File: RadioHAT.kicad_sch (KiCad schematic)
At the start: 37 parts, among them J1 RPi_GPIO, J3 Conn_02x06_Odd_Even, J4 Conn_02x07_Odd_Even, U1 INA219AxD, U2 LP3855-ADJ

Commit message: Rename footprint to match filter
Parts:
- R20: footprint RadioHAT:3362P1200LF -> RadioHAT:Potentiometer_Bourns_3362P1200LF
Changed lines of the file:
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@@
 			)
 		)
-		(property "Footprint" "RadioHAT:3362P1200LF"
+		(property "Footprint" "RadioHAT:Potentiometer_Bourns_3362P1200LF"
 			(at 91.44 151.13 0)
 			(effects

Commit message: Implemented @RemyChatel recommendations
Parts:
- removed C4, C5: 10u, Capacitor_Tantalum_SMD:CP_EIA-3216-18_Kemet-A, symbol Device:C_Polarized
- removed J3: Conn_02x06_Odd_Even, Connector_PinHeader_2.54mm:PinHeader_2x06_P2.54mm_Vertical, symbol Connector_Generic:Conn_02x06_Odd_Even
- removed JP4: SolderJumper_2_Open, Jumper:SolderJumper-2_P1.3mm_Open_Pad1.0x1.5mm, symbol Jumper:SolderJumper_2_Open
- added C4, C5: 100n, Capacitor_SMD:C_0805_2012Metric_Pad1.18x1.45mm_HandSolder, symbol Device:C
- added J3: Conn_02x07_Odd_Even, Connector_PinHeader_2.54mm:PinHeader_2x07_P2.54mm_Vertical, symbol Connector_Generic:Conn_02x07_Odd_Even
- R14: footprint Resistor_SMD:R_2816_7142Metric_Pad3.20x4.45mm_HandSolder -> RadioHAT:R_2512_6332Metric_Pad1.40x3.35mm_HandSolder_Bypass; Mouser 71-WSHP2818R1000FEA -> 588-PCS2512DR1000ET
- R19: value 100R -> 10k; Tolerance (none) -> 1%
- R20: value 18R -> 2k
- R21: value 51R -> 6.8k; Tolerance (none) -> 1%
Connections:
- net +5V: now also C4.1
- net GND: now also C4.2, C5.2, J3.1 (Pin_1), J3.2 (Pin_2)
- net MISO: now also J3.11 (Pin_11)
- net MOSI: now also J3.13 (Pin_13)
- net NSS0: now also J3.7 (Pin_7)
- net SCK: now also J3.9 (Pin_9)
- net SCL: now also J3.5 (Pin_5)
- net SCL_SENSE: now also J1.10 (BCM15_RXD), R2.2; no longer J1.8 (BCM14_TXD), R1.2
- net SDA: now also J3.3 (Pin_3)
- net SDA_SENSE: now also J1.8 (BCM14_TXD), R1.2; no longer J1.10 (BCM15_RXD), R2.2
- net at JP5.1 (A), R19.1, U2.3 (VOUT): now also C5.1
- net at R1.1: now also J3.4 (Pin_4)
- net at R2.1: now also J3.6 (Pin_6)
- net at R5.1: now also J3.12 (Pin_12)
- net at R6.1: now also J3.14 (Pin_14)
- net at R3.1: now also J3.8 (Pin_8)
- net at R4.1: now also J3.10 (Pin_10)
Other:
- note added: "V_out = 1.216 * (1 + R1/R2) max(V_out) < 3.6 V (absolute max for most modules) min(V_out) > 3.0 V (brownout) R2 = R1/((V_out/1.216) - 1) For R1 = 10k ohm and max(V_out): R2 = 10e3/((3.6/1.216) - 1) = 5.1 kohm For min(V_out) R2 = 10e3/((3.0/1.216) - 1) = 6.816 kohm, round to 6.8 kohm R2_pot = 5.1 - 6.8 = 1.7 kohm, round to 2 kohm max(V_out) = 1.216 * (1 + 10e3/5.1e3) = 3.60 V min(V_out) = 1.216 * 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"
- note removed: "V_out = 1.216 * (1 + R1/R2) max(V_out) < 3.6 V (absolute max for most modules) min(V_out) > 3.0 V (brownout) R2 = R1/((V_out/1.216) - 1) For R1 = 100 ohm and max(V_out): R2 = 100/((3.6/1.216) - 1) = 51 ohm For min(V_out) R2 = 100/((3.0/1.216) - 1) = 68.16 ohm, round up to 70 ohm R2_pot = 51 - 70 = 20 ohm max(V_out) = 3.60 V min(V_out) = 2.93 V"

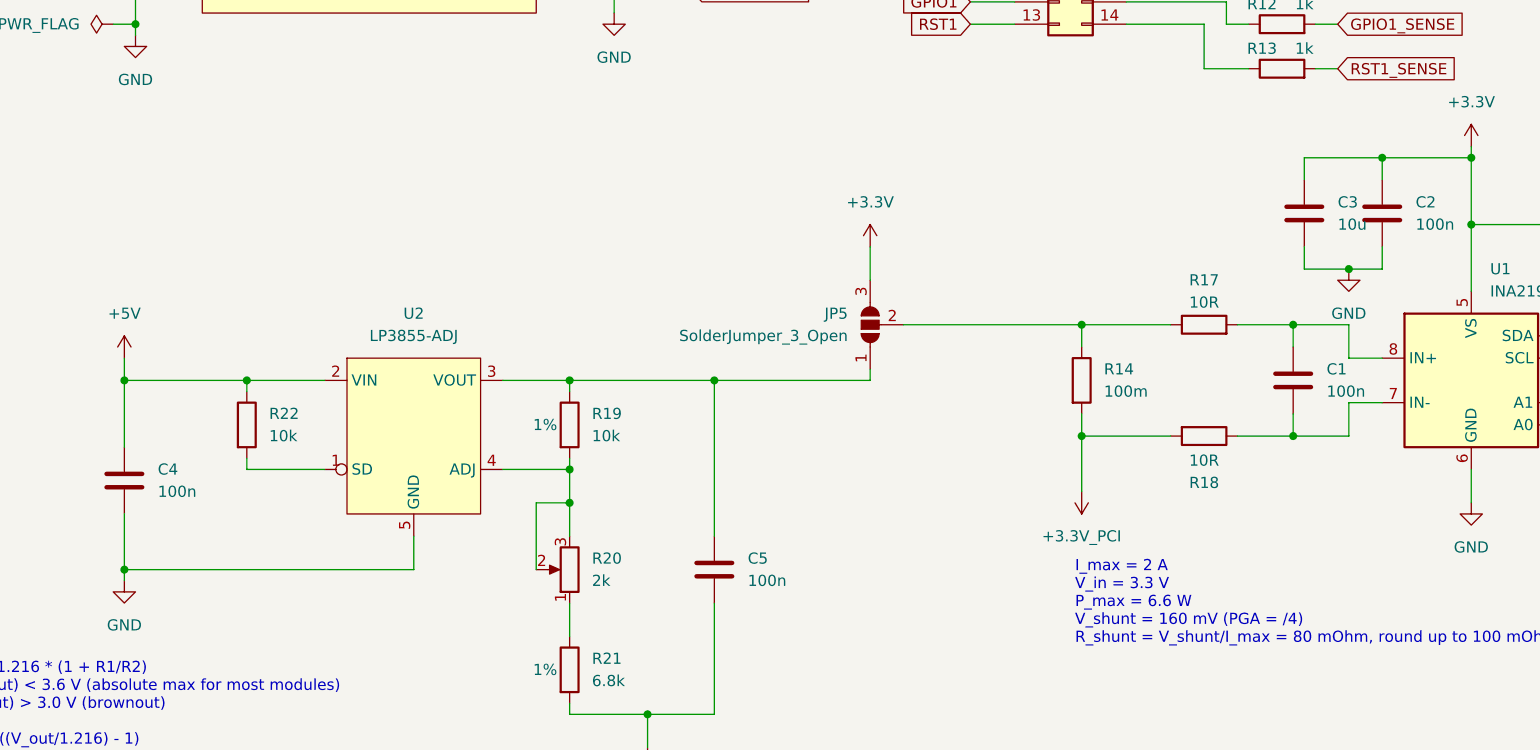
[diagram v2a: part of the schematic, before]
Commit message: [SCH] Add Mouser part numbers
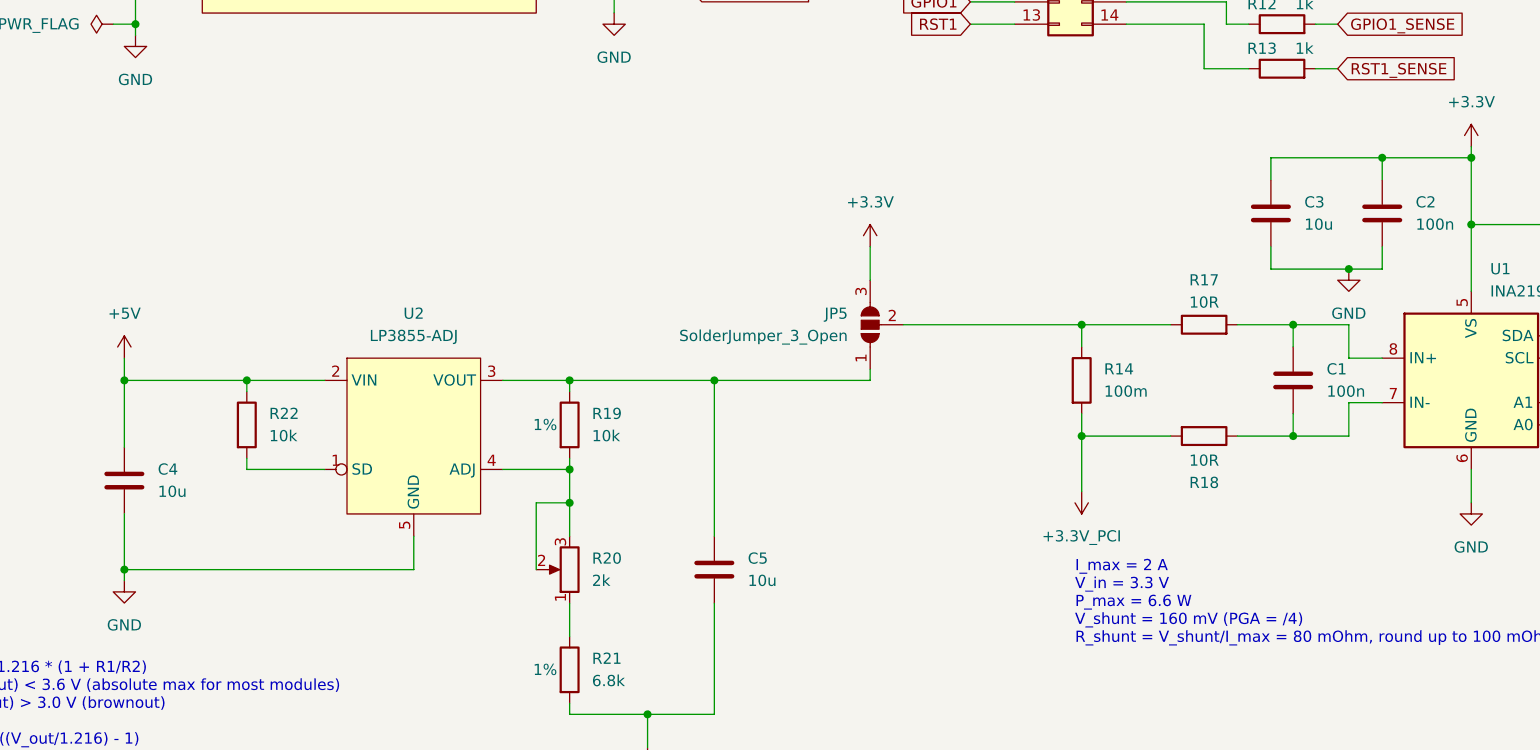
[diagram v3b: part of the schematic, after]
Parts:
- C3: footprint Capacitor_SMD:C_0603_1608Metric_Pad1.08x0.95mm_HandSolder -> Capacitor_SMD:C_0805_2012Metric_Pad1.18x1.45mm_HandSolder; Mouser (none) -> 581-KAM21AR71A106MU
- C4, C5: value 100n -> 10u
- R15, R16, R19, R22: Mouser (none) -> 603-AF0603FR-0710KL
- R17: Mouser (none) -> 71-CRCW060310R0FKEAC
- R21: Mouser (none) -> 603-RC0603FR-106K8L
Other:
- moved on the sheet: C3
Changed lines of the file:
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@@
 	(wire
 		(pts
-			(xy 175.26 116.84) (xy 180.34 116.84)
+			(xy 171.45 116.84) (xy 180.34 116.84)
 		)
 		(stroke
@@
 	(wire
 		(pts
-			(xy 175.26 114.3) (xy 175.26 116.84)
+			(xy 171.45 114.3) (xy 171.45 116.84)
 		)
 		(stroke
@@
 	(wire
 		(pts
-			(xy 175.26 106.68) (xy 175.26 104.14)
+			(xy 171.45 106.68) (xy 171.45 104.14)
 		)
 		(stroke
@@
 	(wire
 		(pts
-			(xy 175.26 104.14) (xy 184.15 104.14)
+			(xy 171.45 104.14) (xy 184.15 104.14)
 		)
 		(stroke
@@
 			)
 		)
+		(property "Mouser" "603-AF0603FR-0710KL"
+			(at 210.82 116.84 0)
+			(effects
+				(font
+					(size 1.27 1.27)
+				)
+				(hide yes)
+			)
+		)
 		(pin "1"
 		)
@@
 			)
 		)
+		(property "Mouser" "71-CRCW060310R0FKEAC"
+			(at 163.83 123.19 90)
+			(effects
+				(font
+					(size 1.27 1.27)
+				)
+				(hide yes)
+			)
+		)
 		(pin "1"
 		)
@@
 			)
 		)
+		(property "Mouser" "603-AF0603FR-0710KL"
+			(at 91.44 134.62 0)
+			(effects
+				(font
+					(size 1.27 1.27)
+				)
+				(hide yes)
+			)
+		)
 		(pin "1"
 		)
@@
 			)
 		)
+		(property "Mouser" "603-RC0603FR-106K8L"
+			(at 91.44 162.56 0)
+			(effects
+				(font
+					(size 1.27 1.27)
+				)
+				(hide yes)
+			)
+		)
 		(pin "1"
 		)
@@
 			)
 		)
+		(property "Mouser" "603-AF0603FR-0710KL"
+			(at 219.71 116.84 0)
+			(effects
+				(font
+					(size 1.27 1.27)
+				)
+				(hide yes)
+			)
+		)
 		(pin "1"
 		)
@@
 			)
 		)
-		(property "Value" "100n"
+		(property "Value" "10u"
 			(at 111.76 152.3999 0)
 			(effects
@@
 	(symbol
 		(lib_id "Device:C")
-		(at 175.26 110.49 0)
+		(at 171.45 110.49 0)
 		(unit 1)
 		(exclude_from_sim no)
@@
 		(fields_autoplaced yes)
 		(property "Reference" "C3"
-			(at 179.07 109.2199 0)
+			(at 175.26 109.2199 0)
 			(effects
 				(font
@@
 		)
 		(property "Value" "10u"
-			(at 179.07 111.7599 0)
+			(at 175.26 111.7599 0)
 			(effects
 				(font
@@
 			)
 		)
-		(property "Footprint" "Capacitor_SMD:C_0603_1608Metric_Pad1.08x0.95mm_HandSolder"
-			(at 176.2252 114.3 0)
+		(property "Footprint" "Capacitor_SMD:C_0805_2012Metric_Pad1.18x1.45mm_HandSolder"
+			(at 172.4152 114.3 0)
 			(effects
 				(font
@@
 		)
 		(property "Datasheet" "~"
-			(at 175.26 110.49 0)
+			(at 171.45 110.49 0)
 			(effects
 				(font
@@
 		)
 		(property "Description" "Unpolarized capacitor"
-			(at 175.26 110.49 0)
+			(at 171.45 110.49 0)
+			(effects
+				(font
+					(size 1.27 1.27)
+				)
+				(hide yes)
+			)
+		)
+		(property "Mouser" "581-KAM21AR71A106MU"
+			(at 171.45 110.49 0)
 			(effects
 				(font
@@
 			)
 		)
+		(property "Mouser" "603-AF0603FR-0710KL"
+			(at 54.61 134.62 0)
+			(effects
+				(font
+					(size 1.27 1.27)
+				)
+				(hide yes)
+			)
+		)
 		(pin "1"
 		)
@@
 			)
 		)
-		(property "Value" "100n"
+		(property "Value" "10u"
 			(at 44.45 142.2399 0)
 			(effects

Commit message: Add last remaining Mouser part numbers
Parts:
- C1, C2: Mouser (none) -> 963-MAJCU168BB7104KT
- J1: Mouser (none) -> 200-SSQ12004TD
- J2: Mouser (none) -> 571-1775838-2
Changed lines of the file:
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@@
+			)
+		)
+		(property "Mouser" "963-MAJCU168BB7104KT"
+			(at 173.99 129.54 0)
+			(effects
+				(font
+					(size 1.27 1.27)
+				)
+				(hide yes)
 			)
 		)
@@
 			)
 		)
+		(property "Mouser" "200-SSQ12004TD"
+			(at 67.31 31.75 0)
+			(effects
+				(font
+					(size 1.27 1.27)
+				)
+				(hide yes)
+			)
+		)
 		(pin "35"
 		)
@@
 			)
 		)
+		(property "Mouser" "963-MAJCU168BB7104KT"
+			(at 184.15 110.49 0)
+			(effects
+				(font
+					(size 1.27 1.27)
+				)
+				(hide yes)
+			)
+		)
 		(pin "1"
 		)
@@
 			(effects
 				(font
+					(size 1.27 1.27)
+				)
+				(hide yes)
+			)
+		)
+		(property "Mouser" "571-1775838-2"
+			(at 246.38 66.04 0)
+			(effects
+				(font

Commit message: Fix LDO feedback resistors values and part numbers
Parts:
- R20: Mouser 652-3362P-1-200LF -> 652-3362P-1-202LF
- R21: value 6.8k -> 5.1k; Mouser 603-RC0603FR-106K8L -> 279-CRG0603F5K1
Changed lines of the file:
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@@
 			)
 		)
-		(property "Value" "6.8k"
+		(property "Value" "5.1k"
 			(at 93.98 163.8299 0)
 			(effects
@@
 			)
 		)
-		(property "Mouser" "603-RC0603FR-106K8L"
+		(property "Mouser" "279-CRG0603F5K1"
 			(at 91.44 162.56 0)
 			(effects
@@
 			)
 		)
-		(property "Mouser" "652-3362P-1-200LF"
+		(property "Mouser" "652-3362P-1-202LF"
 			(at 91.44 151.13 0)
 			(effects

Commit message: [SCH] Move I2C address selection jumpers to 3V3 to simplify layout
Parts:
- J2: footprint RadioHAT:Mini_PCIe_Latch -> RadioHAT:Mini_PCIe_Latch_Hole
- R1, R10, R11, R12, R13, R2, R3, R4, R5, R6, R7, R8, R9: footprint Resistor_SMD:R_0805_2012Metric_Pad1.20x1.40mm_HandSolder -> Resistor_SMD:R_0603_1608Metric_Pad0.98x0.95mm_HandSolder
- renumbered R22 to R19, R19 to R20, R20 to R21, R21 to R22
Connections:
- net +3.3V: now also JP1.3 (B), JP2.3 (B)
- net SCL: no longer JP2.3 (B)
- net SDA: no longer JP1.3 (B)
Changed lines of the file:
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@@
 	)
 	(junction
+		(at 219.71 111.76)
+		(diameter 0)
+		(color 0 0 0 0)
+	)
+	(junction
 		(at 270.51 78.74)
 		(diameter 0)
@@
 	)
 	(junction
-		(at 227.33 127)
-		(diameter 0)
-		(color 0 0 0 0)
-	)
-	(junction
 		(at 91.44 143.51)
 		(diameter 0)
@@
 	)
 	(junction
-		(at 215.9 124.46)
-		(diameter 0)
-		(color 0 0 0 0)
-	)
-	(junction
 		(at 210.82 111.76)
 		(diameter 0)
@@
 	)
 	(junction
+		(at 215.9 111.76)
+		(diameter 0)
+		(color 0 0 0 0)
+	)
+	(junction
 		(at 96.52 52.07)
 		(diameter 0)
@@
 	(wire
 		(pts
+			(xy 210.82 111.76) (xy 215.9 111.76)
+		)
+		(stroke
+			(width 0)
+			(type default)
+		)
+	)
+	(wire
+		(pts
 			(xy 92.71 52.07) (xy 96.52 52.07)
 		)
@@
 	(wire
 		(pts
-			(xy 219.71 127) (xy 227.33 127)
+			(xy 219.71 127) (xy 234.95 127)
 		)
 		(stroke
@@
 	(wire
 		(pts
+			(xy 210.82 124.46) (xy 234.95 124.46)
+		)
+		(stroke
+			(width 0)
+			(type default)
+		)
+	)
+	(wire
+		(pts
 			(xy 31.75 54.61) (xy 44.45 54.61)
 		)
@@
 	(wire
 		(pts
+			(xy 215.9 111.76) (xy 215.9 133.35)
+		)
+		(stroke
+			(width 0)
+			(type default)
+		)
+	)
+	(wire
+		(pts
 			(xy 92.71 36.83) (xy 96.52 36.83)
 		)
@@
 	(wire
 		(pts
-			(xy 227.33 127) (xy 234.95 127)
-		)
-		(stroke
-			(width 0)
-			(type default)
-		)
-	)
-	(wire
-		(pts
 			(xy 267.97 76.2) (xy 270.51 76.2)
 		)
@@
 	(wire
 		(pts
-			(xy 210.82 124.46) (xy 215.9 124.46)
-		)
-		(stroke
-			(width 0)
-			(type default)
-		)
-	)
-	(wire
-		(pts
 			(xy 166.37 86.36) (xy 166.37 88.9)
 		)
@@
 	(wire
 		(pts
-			(xy 240.03 95.25) (xy 242.57 95.25)
+			(xy 227.33 111.76) (xy 219.71 111.76)
 		)
 		(stroke
@@
 	(wire
 		(pts
-			(xy 166.37 45.72) (xy 166.37 43.18)
+			(xy 240.03 95.25) (xy 242.57 95.25)
 		)
 		(stroke
@@
 	(wire
 		(pts
-			(xy 210.82 111.76) (xy 219.71 111.76)
+			(xy 166.37 45.72) (xy 166.37 43.18)
 		)
 		(stroke
@@
 	(wire
 		(pts
+			(xy 227.33 133.35) (xy 227.33 111.76)
+		)
+		(stroke
+			(width 0)
+			(type default)
+		)
+	)
+	(wire
+		(pts
 			(xy 171.45 106.68) (xy 171.45 104.14)
 		)
@@
 	(wire
 		(pts
-			(xy 215.9 124.46) (xy 215.9 133.35)
-		)
-		(stroke
-			(width 0)
-			(type default)
-		)
-	)
-	(wire
-		(pts
 			(xy 137.16 86.36) (xy 142.24 86.36)
 		)
@@
 	(wire
 		(pts
+			(xy 215.9 111.76) (xy 219.71 111.76)
+		)
+		(stroke
+			(width 0)
+			(type default)
+		)
+	)
+	(wire
+		(pts
 			(xy 96.52 59.69) (xy 96.52 72.39)
 		)
@@
 	(wire
 		(pts
-			(xy 215.9 124.46) (xy 234.95 124.46)
-		)
-		(stroke
-			(width 0)
-			(type default)
-		)
-	)
-	(wire
-		(pts
 			(xy 176.53 78.74) (xy 179.07 78.74)
 		)
@@
 	(wire
 		(pts
-			(xy 227.33 127) (xy 227.33 133.35)
-		)
-		(stroke
-			(width 0)
-			(type default)
-		)
-	)
-	(wire
-		(pts
 			(xy 184.15 114.3) (xy 184.15 116.84)
 		)
@@
 			)
 		)
-		(property "Footprint" "Resistor_SMD:R_0805_2012Metric_Pad1.20x1.40mm_HandSolder"
+		(property "Footprint" "Resistor_SMD:R_0603_1608Metric_Pad0.98x0.95mm_HandSolder"
 			(at 172.72 90.678 90)
 			(effects
@@
 			)
 		)
-		(property "Footprint" "Resistor_SMD:R_0805_2012Metric_Pad1.20x1.40mm_HandSolder"
+		(property "Footprint" "Resistor_SMD:R_0603_1608Metric_Pad0.98x0.95mm_HandSolder"
 			(at 172.72 34.798 90)
 			(effects
@@
 			)
 		)
-		(property "Footprint" "Resistor_SMD:R_0805_2012Metric_Pad1.20x1.40mm_HandSolder"
+		(property "Footprint" "Resistor_SMD:R_0603_1608Metric_Pad0.98x0.95mm_HandSolder"
 			(at 172.72 39.878 90)
 			(effects
@@
 		(on_board yes)
 		(dnp no)
-		(property "Reference" "R19"
+		(property "Reference" "R20"
 			(at 93.98 133.3499 0)
 			(effects
@@
 			(project "RadioHAT"
 				(path "/b81b30b5-0f95-4689-93f2-268be91e8e59"
-					(reference "R19")
+					(reference "R20")
 					(unit 1)
 				)
@@
 			)
 		)
-		(property "Footprint" "Resistor_SMD:R_0805_2012Metric_Pad1.20x1.40mm_HandSolder"
+		(property "Footprint" "Resistor_SMD:R_0603_1608Metric_Pad0.98x0.95mm_HandSolder"
 			(at 172.72 85.598 90)
 			(effects
@@
 			)
 		)
-		(property "Footprint" "Resistor_SMD:R_0805_2012Metric_Pad1.20x1.40mm_HandSolder"
+		(property "Footprint" "Resistor_SMD:R_0603_1608Metric_Pad0.98x0.95mm_HandSolder"
 			(at 172.72 55.118 90)
 			(effects
@@
 			)
 		)
-		(property "Footprint" "Resistor_SMD:R_0805_2012Metric_Pad1.20x1.40mm_HandSolder"
+		(property "Footprint" "Resistor_SMD:R_0603_1608Metric_Pad0.98x0.95mm_HandSolder"
 			(at 172.72 60.198 90)
 			(effects
@@
 		(on_board yes)
 		(dnp no)
-		(property "Reference" "R21"
+		(property "Reference" "R22"
 			(at 93.98 161.2899 0)
 			(effects
@@
 			(project "RadioHAT"
 				(path "/b81b30b5-0f95-4689-93f2-268be91e8e59"
-					(reference "R21")
+					(reference "R22")
 					(unit 1)
 				)
@@
 			)
 		)
-		(property "Footprint" "Resistor_SMD:R_0805_2012Metric_Pad1.20x1.40mm_HandSolder"
+		(property "Footprint" "Resistor_SMD:R_0603_1608Metric_Pad0.98x0.95mm_HandSolder"
 			(at 172.72 80.518 90)
 			(effects
@@
 			)
 		)
-		(property "Footprint" "Resistor_SMD:R_0805_2012Metric_Pad1.20x1.40mm_HandSolder"
+		(property "Footprint" "Resistor_SMD:R_0603_1608Metric_Pad0.98x0.95mm_HandSolder"
 			(at 172.72 70.358 90)
 			(effects
@@
 			)
 		)
-		(property "Footprint" "Resistor_SMD:R_0805_2012Metric_Pad1.20x1.40mm_HandSolder"
+		(property "Footprint" "Resistor_SMD:R_0603_1608Metric_Pad0.98x0.95mm_HandSolder"
 			(at 172.72 50.038 90)
 			(effects
@@
 			)
 		)
-		(property "Footprint" "Resistor_SMD:R_0805_2012Metric_Pad1.20x1.40mm_HandSolder"
+		(property "Footprint" "Resistor_SMD:R_0603_1608Metric_Pad0.98x0.95mm_HandSolder"
 			(at 172.72 75.438 90)
 			(effects
@@
 			)
 		)
-		(property "Footprint" "Resistor_SMD:R_0805_2012Metric_Pad1.20x1.40mm_HandSolder"
+		(property "Footprint" "Resistor_SMD:R_0603_1608Metric_Pad0.98x0.95mm_HandSolder"
 			(at 172.72 95.758 90)
 			(effects
@@
 			)
 		)
-		(property "Footprint" "Resistor_SMD:R_0805_2012Metric_Pad1.20x1.40mm_HandSolder"
+		(property "Footprint" "Resistor_SMD:R_0603_1608Metric_Pad0.98x0.95mm_HandSolder"
 			(at 172.72 44.958 90)
 			(effects
@@
 		(dnp no)
 		(fields_autoplaced yes)
-		(property "Reference" "R22"
+		(property "Reference" "R19"
 			(at 57.15 133.3499 0)
 			(effects
@@
 			(project "RadioHAT"
 				(path "/b81b30b5-0f95-4689-93f2-268be91e8e59"
-					(reference "R22")
+					(reference "R19")
 					(unit 1)
 				)
@@
 			)
 		)
-		(property "Footprint" "Resistor_SMD:R_0805_2012Metric_Pad1.20x1.40mm_HandSolder"
+		(property "Footprint" "Resistor_SMD:R_0603_1608Metric_Pad0.98x0.95mm_HandSolder"
 			(at 172.72 65.278 90)
 			(effects
@@
 			)
 		)
-		(property "Footprint" "RadioHAT:Mini_PCIe_Latch"
+		(property "Footprint" "RadioHAT:Mini_PCIe_Latch_Hole"
 			(at 251.46 69.85 0)
 			(effects
@@
 		(dnp no)
 		(fields_autoplaced yes)
-		(property "Reference" "R20"
+		(property "Reference" "R21"
 			(at 93.98 149.8599 0)
 			(effects
@@
 			(project ""
 				(path "/b81b30b5-0f95-4689-93f2-268be91e8e59"
-					(reference "R20")
+					(reference "R21")
 					(unit 1)
 				)
